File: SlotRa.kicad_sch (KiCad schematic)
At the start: 30 parts, among them J1 Nice!nano - left pins, J10 Battery Holes, J14 GPS Pins, J2 Nice!nano - right pins, J3 Lora - left pins, J4 Lora - right pins, J5 I2C Oled screen, J6 T1 Drain - SMD, J7 T2 Drain - SMD, J8 T3 Drain - SMD, J9 Battery Connector JST 1.25, SW1 Reset, SW2 SW_Push, T1 SI2312, T2 SI2312, T3 SI2312, U1 XB8089D0

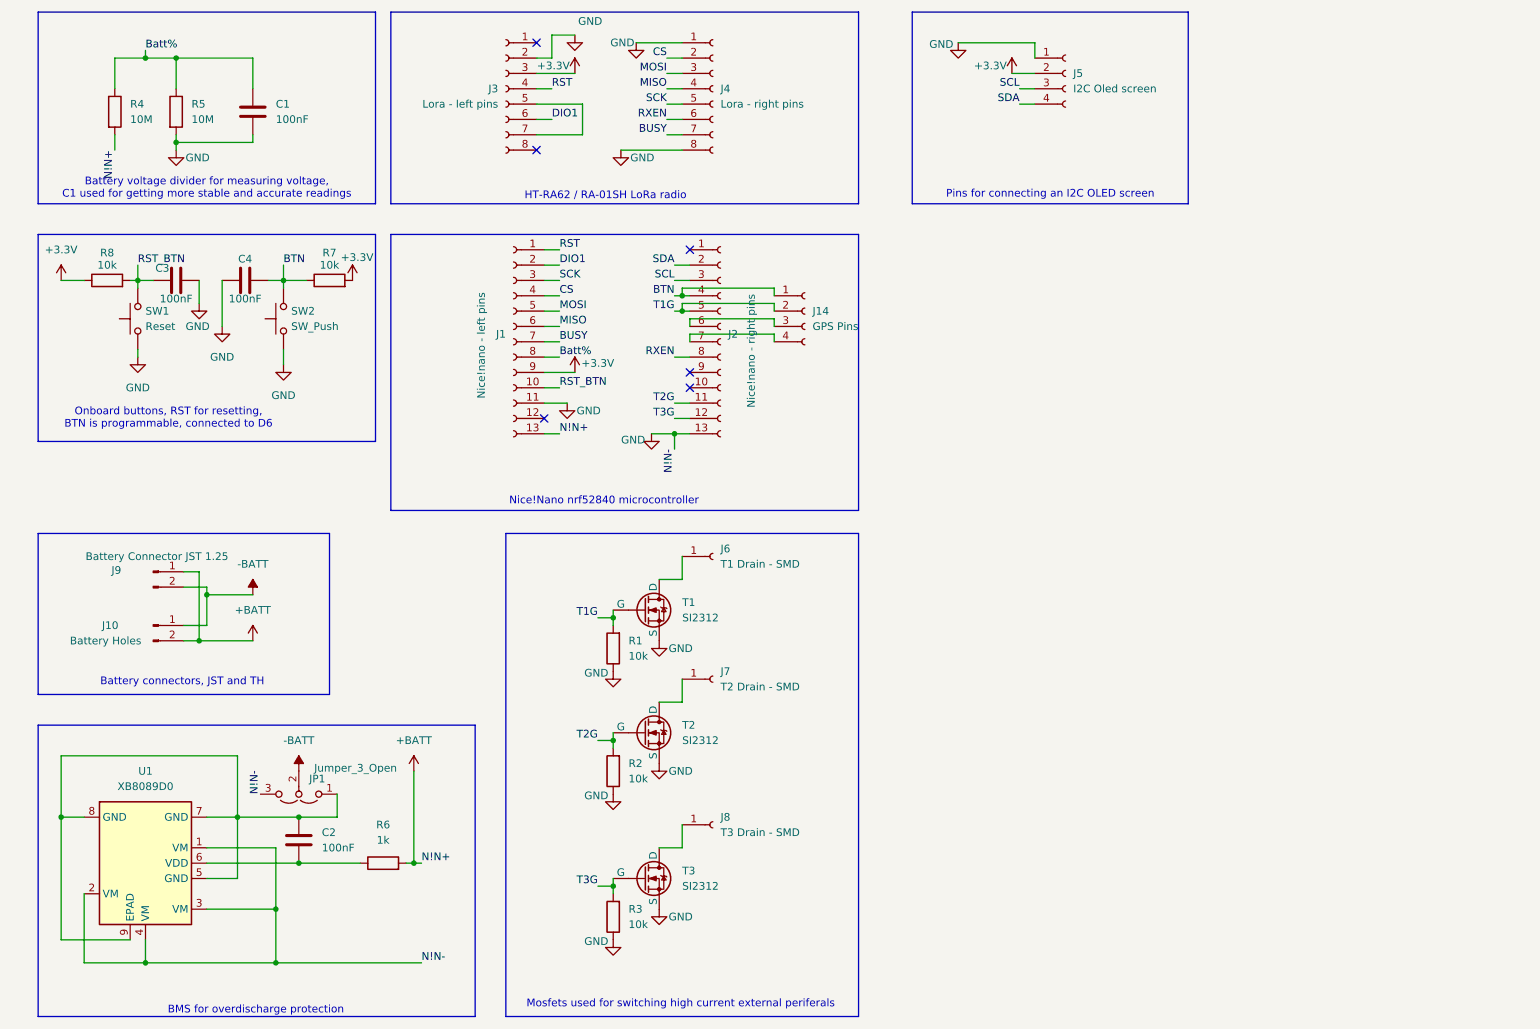
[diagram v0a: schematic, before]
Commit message: Project renaming, cleansing and small additions
Renamed kicad files.
Performed some beautifications in the schematics for a better readability.
Added gate resistors.
Added arbitrary led for notifications.
Added an e-capacitor for the modem powering filtering and stability improvements.
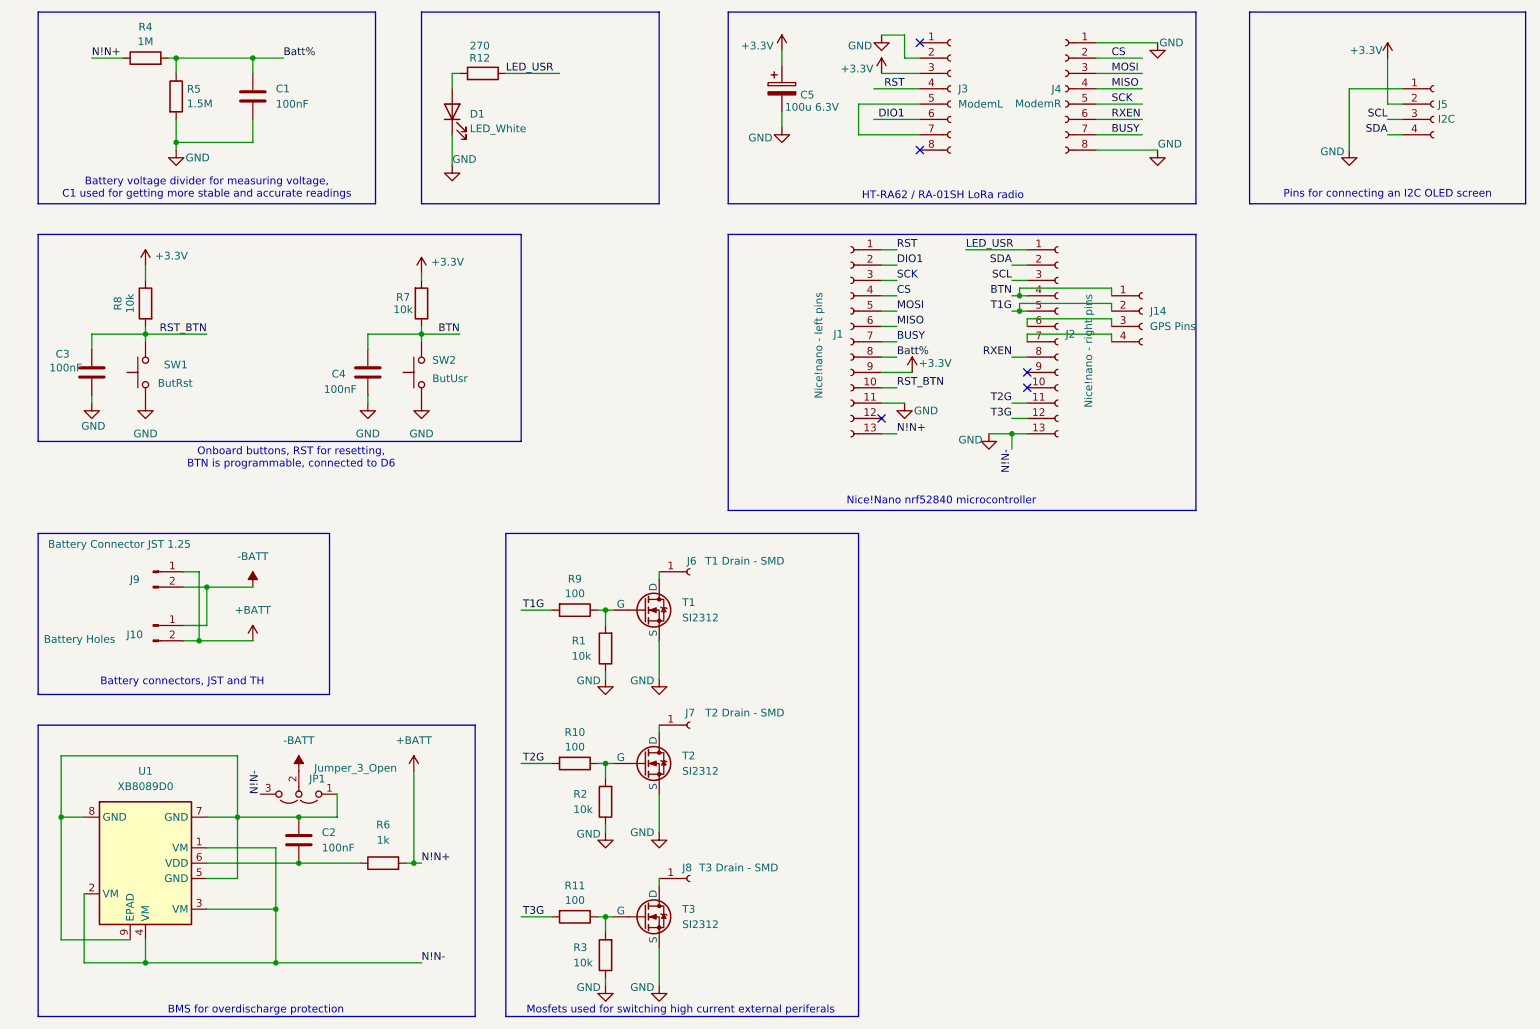
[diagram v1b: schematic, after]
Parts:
- added C5: 100u 6.3V, Capacitor_Tantalum_SMD:CP_EIA-7343-31_Kemet-D, symbol Device:C_Polarized
- added D1: LED_White, LED_THT:LED_D3.0mm_Horizontal_O6.35mm_Z10.0mm, symbol Device:LED
- added R10, R11, R9: 100, Resistor_SMD:R_1206_3216Metric_Pad1.30x1.75mm_HandSolder, symbol Device:R
- added R12: 270, Resistor_SMD:R_1206_3216Metric_Pad1.30x1.75mm_HandSolder, symbol Device:R
- J3: value Lora - left pins -> ModemL
- J4: value Lora - right pins -> ModemR
- J5: value I2C Oled screen -> I2C
- R4: value 10M -> 1M
- R5: value 10M -> 1.5M
- SW1: value Reset -> ButRst
- SW2: value SW_Push -> ButUsr
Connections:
- net +3.3V: now also C5.1
- net +BATT: now also R4.1; no longer R4.2
- net Batt%: now also R4.2; no longer R4.1
- net GND: now also C5.2, D1.1 (K)
- net T1G: now also R9.2; no longer R1.2, T1.2 (G)
- net T2G: now also R10.2; no longer R2.2, T2.2 (G)
- net T3G: now also R11.2; no longer R3.2, T3.2 (G)
- net LED_USR: now reaches J2.1 (Pin_1)
- net LED_USR: now also R12.1
- new net: R11.1, R3.2, T3.2 (G)
- new net: D1.2 (A), R12.2
- new net: R10.1, R2.2, T2.2 (G)
- new net: R1.2, R9.1, T1.2 (G)
- no-connect marks 6 -> 5
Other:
- title: fakeTec v5 -> SlotRa (fakeTec_v5 mod)
- moved on the sheet: C1, C3, C4, J1, J14, J2, J3, J4, J5, J6, J7, J8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

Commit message: Honey, I Shrunk The Footprints
1206 caps and ress are 0805 now. They're cheaper, have suitable voltage and power ratings, and are still easy to solder.
Also the author have a bunch of them, but not the 1206 ones...
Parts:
- C1, C2, C3, C4: footprint Capacitor_SMD:C_1206_3216Metric_Pad1.33x1.80mm_HandSolder -> Capacitor_SMD:C_0805_2012Metric_Pad1.18x1.45mm_HandSolder
- R1, R10, R11, R12, R2, R3, R4, R5, R6, R7, R8, R9: footprint Resistor_SMD:R_1206_3216Metric_Pad1.30x1.75mm_HandSolder -> Resistor_SMD:R_0805_2012Metric_Pad1.20x1.40mm_HandSolder
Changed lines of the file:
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@@
 			)
 		)
-		(property "Footprint" "Resistor_SMD:R_1206_3216Metric_Pad1.30x1.75mm_HandSolder"
+		(property "Footprint" "Resistor_SMD:R_0805_2012Metric_Pad1.20x1.40mm_HandSolder"
 			(at 76.2 160.528 90)
 			(effects
@@
 			)
 		)
-		(property "Footprint" "Resistor_SMD:R_1206_3216Metric_Pad1.30x1.75mm_HandSolder"
+		(property "Footprint" "Resistor_SMD:R_0805_2012Metric_Pad1.20x1.40mm_HandSolder"
 			(at 40.132 31.75 90)
 			(effects
@@
 			)
 		)
-		(property "Footprint" "Capacitor_SMD:C_1206_3216Metric_Pad1.33x1.80mm_HandSolder"
+		(property "Footprint" "Capacitor_SMD:C_0805_2012Metric_Pad1.18x1.45mm_HandSolder"
 			(at 55.5752 35.56 0)
 			(effects
@@
 			)
 		)
-		(property "Footprint" "Resistor_SMD:R_1206_3216Metric_Pad1.30x1.75mm_HandSolder"
+		(property "Footprint" "Resistor_SMD:R_0805_2012Metric_Pad1.20x1.40mm_HandSolder"
 			(at 92.71 29.718 90)
 			(effects
@@
 			)
 		)
-		(property "Footprint" "Resistor_SMD:R_1206_3216Metric_Pad1.30x1.75mm_HandSolder"
+		(property "Footprint" "Resistor_SMD:R_0805_2012Metric_Pad1.20x1.40mm_HandSolder"
 			(at 36.83 27.178 90)
 			(effects
@@
 			)
 		)
-		(property "Footprint" "Resistor_SMD:R_1206_3216Metric_Pad1.30x1.75mm_HandSolder"
+		(property "Footprint" "Resistor_SMD:R_0805_2012Metric_Pad1.20x1.40mm_HandSolder"
 			(at 107.95 165.862 90)
 			(effects
@@
 			)
 		)
-		(property "Footprint" "Resistor_SMD:R_1206_3216Metric_Pad1.30x1.75mm_HandSolder"
+		(property "Footprint" "Resistor_SMD:R_0805_2012Metric_Pad1.20x1.40mm_HandSolder"
 			(at 114.808 173.99 90)
 			(effects
@@
 			)
 		)
-		(property "Footprint" "Resistor_SMD:R_1206_3216Metric_Pad1.30x1.75mm_HandSolder"
+		(property "Footprint" "Resistor_SMD:R_0805_2012Metric_Pad1.20x1.40mm_HandSolder"
 			(at 38.608 66.04 90)
 			(effects
@@
 			)
 		)
-		(property "Footprint" "Capacitor_SMD:C_1206_3216Metric_Pad1.33x1.80mm_HandSolder"
+		(property "Footprint" "Capacitor_SMD:C_0805_2012Metric_Pad1.18x1.45mm_HandSolder"
 			(at 72.6948 73.66 0)
 			(effects
@@
 			)
 		)
-		(property "Footprint" "Resistor_SMD:R_1206_3216Metric_Pad1.30x1.75mm_HandSolder"
+		(property "Footprint" "Resistor_SMD:R_0805_2012Metric_Pad1.20x1.40mm_HandSolder"
 			(at 107.95 140.462 90)
 			(effects
@@
 			)
 		)
-		(property "Footprint" "Resistor_SMD:R_1206_3216Metric_Pad1.30x1.75mm_HandSolder"
+		(property "Footprint" "Resistor_SMD:R_0805_2012Metric_Pad1.20x1.40mm_HandSolder"
 			(at 114.808 148.59 90)
 			(effects
@@
 			)
 		)
-		(property "Footprint" "Resistor_SMD:R_1206_3216Metric_Pad1.30x1.75mm_HandSolder"
+		(property "Footprint" "Resistor_SMD:R_0805_2012Metric_Pad1.20x1.40mm_HandSolder"
 			(at 80.772 66.04 90)
 			(effects
@@
 			)
 		)
-		(property "Footprint" "Resistor_SMD:R_1206_3216Metric_Pad1.30x1.75mm_HandSolder"
+		(property "Footprint" "Resistor_SMD:R_0805_2012Metric_Pad1.20x1.40mm_HandSolder"
 			(at 114.808 123.19 90)
 			(effects
@@
 			)
 		)
-		(property "Footprint" "Resistor_SMD:R_1206_3216Metric_Pad1.30x1.75mm_HandSolder"
+		(property "Footprint" "Resistor_SMD:R_0805_2012Metric_Pad1.20x1.40mm_HandSolder"
 			(at 107.95 115.062 90)
 			(effects
@@
 			)
 		)
-		(property "Footprint" "Capacitor_SMD:C_1206_3216Metric_Pad1.33x1.80mm_HandSolder"
+		(property "Footprint" "Capacitor_SMD:C_0805_2012Metric_Pad1.18x1.45mm_HandSolder"
 			(at 26.9748 81.28 0)
 			(effects
@@
 			)
 		)
-		(property "Footprint" "Capacitor_SMD:C_1206_3216Metric_Pad1.33x1.80mm_HandSolder"
+		(property "Footprint" "Capacitor_SMD:C_0805_2012Metric_Pad1.18x1.45mm_HandSolder"
 			(at 63.1952 158.75 0)
 			(effects

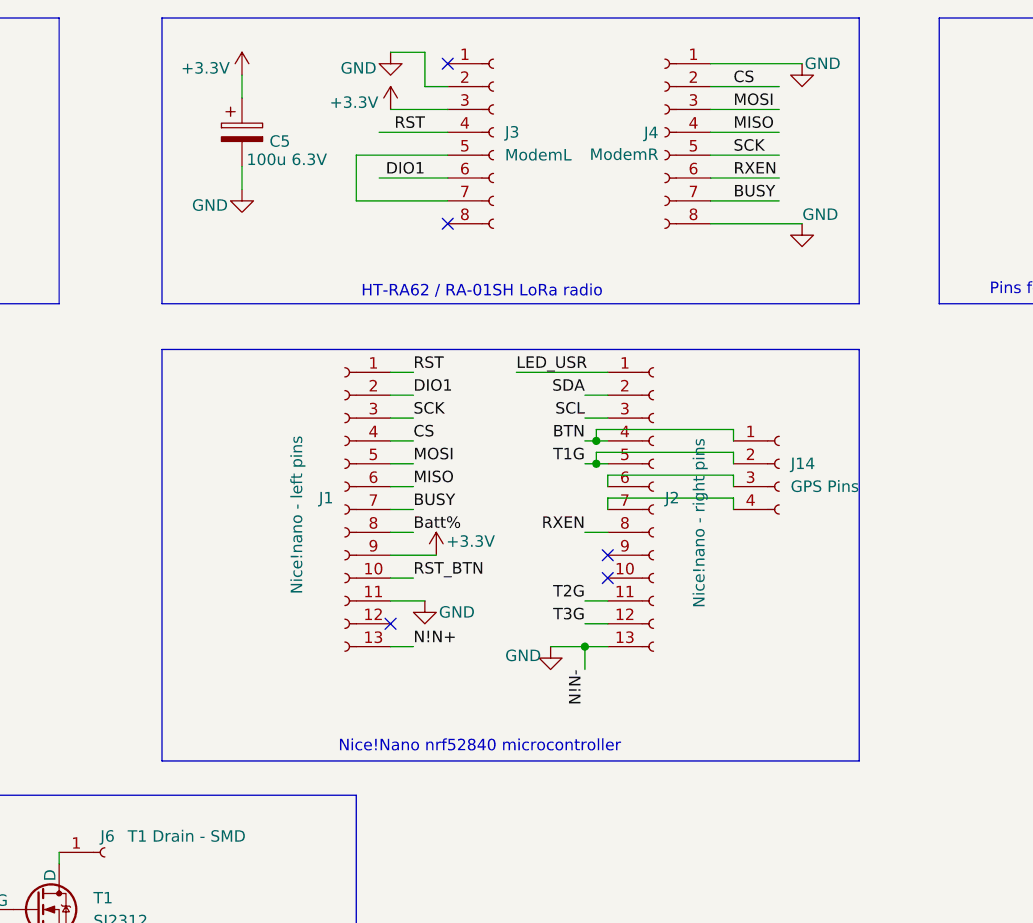
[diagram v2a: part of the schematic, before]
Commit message: TXEN - DIO2 jumper
It is unknown why these modem pads are hard-connected. If one needs this behavior - there is a jumper for it now.
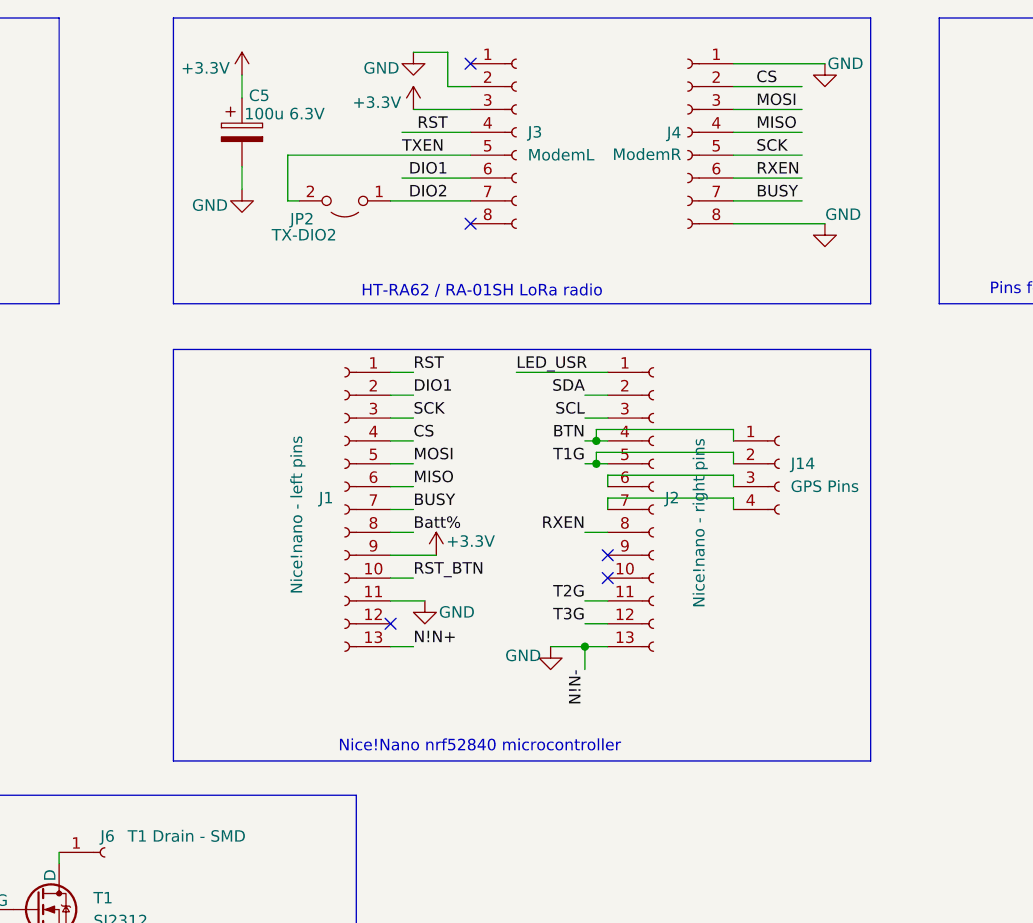
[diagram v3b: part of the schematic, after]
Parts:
- added JP2: TX-DIO2, Jumper:SolderJumper-2_P1.3mm_Open_RoundedPad1.0x1.5mm, symbol Jumper:Jumper_2_Open
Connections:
- net DIO2: now reaches J3.7 (Pin_7)
- net DIO2: now also JP2.1 (A); no longer J3.5 (Pin_5)
- new net TXEN: J3.5 (Pin_5), JP2.2 (B)
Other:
- moved on the sheet: J3, J4
